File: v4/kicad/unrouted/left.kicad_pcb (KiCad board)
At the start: 2 copper layers, 158 x 118.6 mm, 67 parts

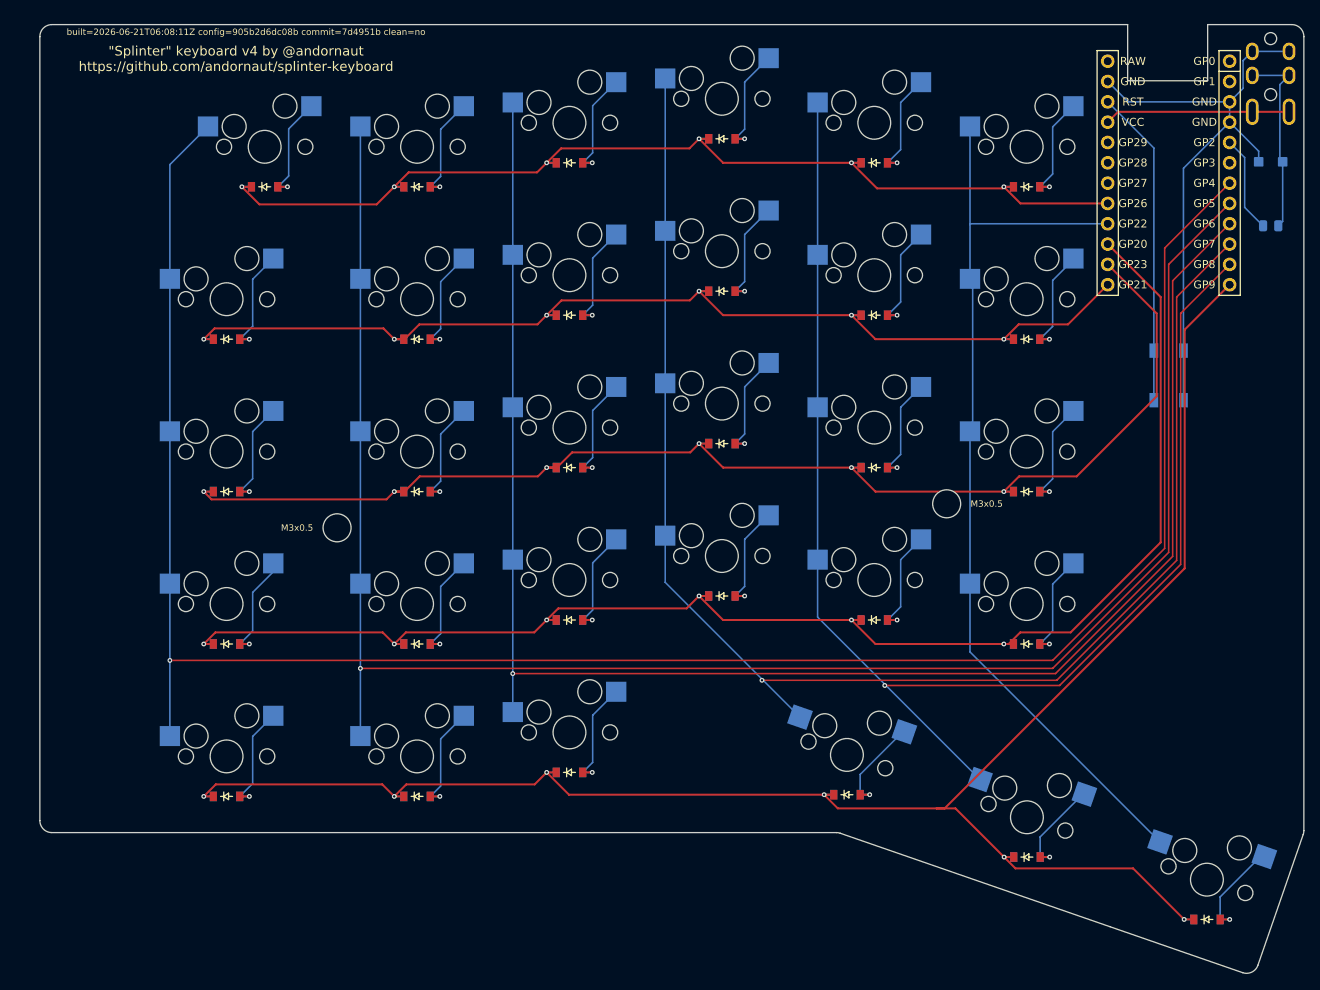
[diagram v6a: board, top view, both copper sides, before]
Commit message: v4: rebuild all boards against current config (footprint cleanups)
Full pipeline rebuild brings unrouted/ + routed/ to config=9096bb80de4e,
reflecting the recent footprint cleanups (lib prefix, side-derived via
layers, dead param). Orphaned include_traces_vias dead stubs removed
(left 385->309 segments / 65->35 vias; right 406->334 / 70->38).
Routing complete: both routed halves pass connectivity DRC (0 violations,
0 unconnected). Teardrops preserved (left 470, right ~500).
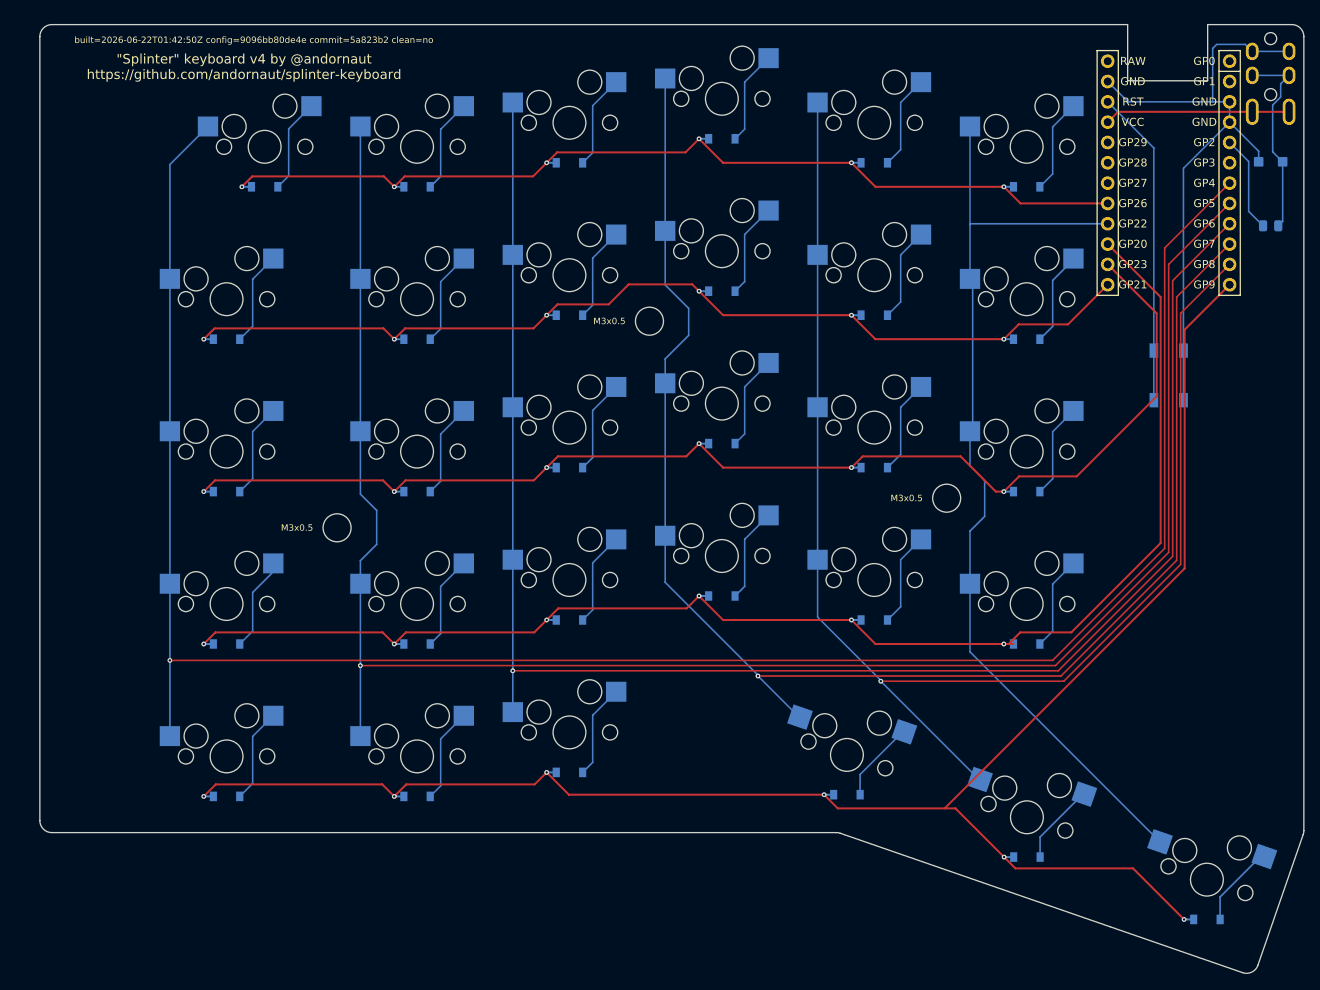
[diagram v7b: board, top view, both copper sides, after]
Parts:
- added MH3: , ceoloide:mounting_hole_npth, F.Cu at (207.1, 126.6)
- MCU1: footprint ceoloide:mcu_liatris -> splinter:mcu_liatris
- moved MH2 0.70 mm to (244.2, 148.7)
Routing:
- net P9: track 228.3 -> 220.1 mm
- net P18: track 130.5 -> 122.3 mm
- net P10: track 136.3 -> 129.8 mm
- net P14: track 186.1 -> 180.1 mm
- net P16: track 163.3 -> 157.6 mm
- net GND: track 74.5 -> 79.2 mm
- net P7: track 187.2 -> 189.8 mm
- net one_upper: track 14.2 -> 11.8 mm, vias 1 -> 0
- net zero_upper: track 14.2 -> 11.8 mm, vias 1 -> 0
- net zero_mod: track 14.2 -> 11.8 mm, vias 1 -> 0
- net zero_lower: track 13.2 -> 10.8 mm, vias 1 -> 0
- net zero_home: track 14.2 -> 11.8 mm, vias 1 -> 0
- net three_mod: track 12.5 -> 10.1 mm, vias 1 -> 0
- net one_num: track 14.2 -> 11.8 mm, vias 1 -> 0
- net one_mod: track 14.2 -> 11.8 mm, vias 1 -> 0
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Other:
- board text added: "DATA"
- board text added: "VCC"
- board text added: "built=2026-06-22T01:42:50Z config=9096bb80de4e commit=5a823b2 clean=no"
- board text removed: "built=2026-06-21T06:08:11Z config=905b2d6dc08b commit=7d4951b clean=no"

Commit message: v4: re-stamp boards clean=yes from committed source (06c8ffa)
Full pipeline rebuild on the now-committed tree: routed + unrouted boards
carry clean=yes commit=06c8ffa, so the provenance stamp is authoritative.
config unchanged (9096bb80de4e). All gates pass: connectivity DRC clean,
GND flood present (master + gerber), full gerber set, BOM/CPL complete,
teardrops 277 left / 295 right. validate:fab passes with zero warnings.
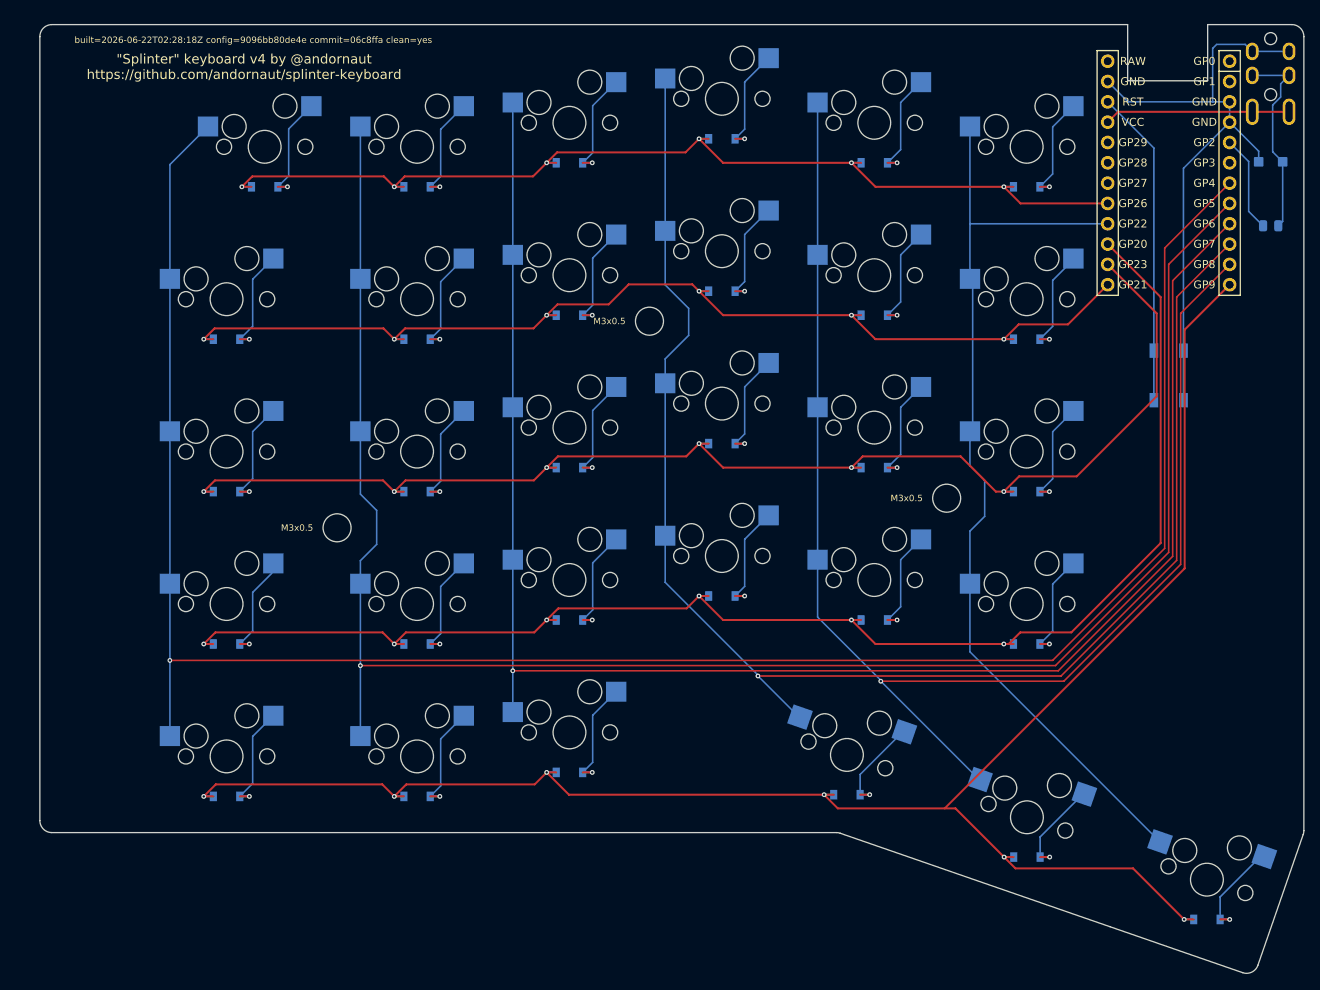
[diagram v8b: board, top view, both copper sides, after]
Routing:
- net P9: track 220.1 -> 227.3 mm
- net P16: track 157.6 -> 164.8 mm
- net P10: track 129.8 -> 137.0 mm
- net P18: track 122.3 -> 129.5 mm
- net P14: track 180.1 -> 186.1 mm
- net one_upper: track 11.8 -> 14.2 mm, vias 0 -> 1
- net zero_mod: track 11.8 -> 14.2 mm, vias 0 -> 1
- net zero_lower: track 10.8 -> 13.2 mm, vias 0 -> 1
- net zero_home: track 11.8 -> 14.2 mm, vias 0 -> 1
- net three_mod: track 10.1 -> 12.5 mm, vias 0 -> 1
- net one_num: track 11.8 -> 14.2 mm, vias 0 -> 1
- net one_mod: track 11.8 -> 14.2 mm, vias 0 -> 1
- net one_lower: track 11.8 -> 14.2 mm, vias 0 -> 1
- net one_home: track 11.8 -> 14.2 mm, vias 0 -> 1
- net four_upper: track 11.8 -> 14.2 mm, vias 0 -> 1
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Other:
- board text added: "built=2026-06-22T02:28:18Z config=9096bb80de4e commit=06c8ffa clean=yes"
- board text removed: "built=2026-06-22T01:42:50Z config=9096bb80de4e commit=5a823b2 clean=no"
